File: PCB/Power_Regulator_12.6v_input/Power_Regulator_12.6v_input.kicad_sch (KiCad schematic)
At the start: 54 parts, among them J1 SE2-30, J2 Jack-DC, U1 TLP3542, U2 TPS55340RTER, U3 TPS563203, U4 TPS54JA20RWWR

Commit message: added test points
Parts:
- added J10, J12, J13, J4, J5, J6, J7, J8, J9: Conn_01x01_Pin, TestPoint:TestPoint_Pad_D1.0mm, symbol Connector:Conn_01x01_Pin
- added J3: Conn_01x05_Pin, Connector_PinHeader_2.54mm:PinHeader_1x05_P2.54mm_Vertical, symbol Connector:Conn_01x05_Pin
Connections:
- net +24V: now also J7.1 (Pin_1)
- net +3.3VA: now also J13.1 (Pin_1), J3.3 (Pin_3), J5.1 (Pin_1)
- net +5V: now also J10.1 (Pin_1), J3.4 (Pin_4), J4.1 (Pin_1)
- net +BATT: now also J3.2 (Pin_2), J8.1 (Pin_1), J9.1 (Pin_1)
- net 24V_RAW: now also J3.5 (Pin_5), J6.1 (Pin_1)
- net GND: now also J3.1 (Pin_1)
- net at R3.2, U1.1: now also J12.1 (Pin_1)

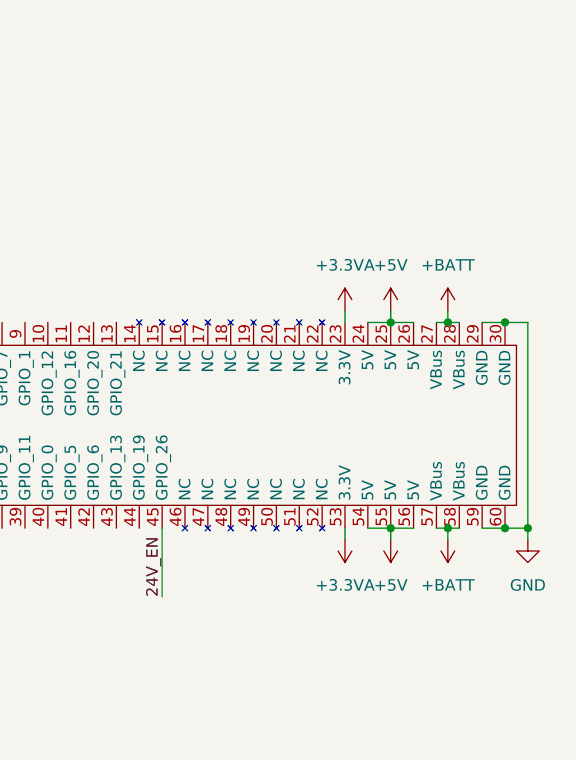
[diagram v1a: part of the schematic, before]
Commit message: added switch footprint
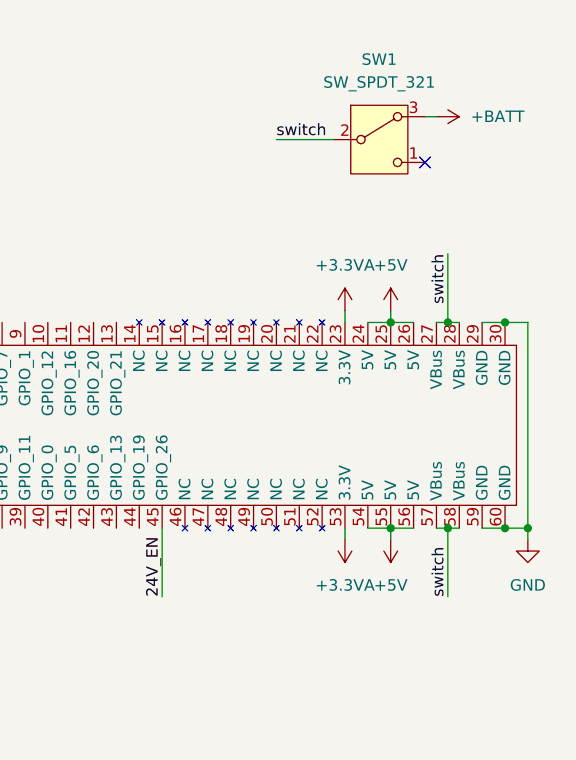
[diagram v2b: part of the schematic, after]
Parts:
- added SW1: SW_SPDT_321, symbol Switch:SW_SPDT_321
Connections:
- net +BATT: now also SW1.3 (A); no longer J1.27 (VBus), J1.28 (VBus), J1.57 (VBus), J1.58 (VBus)
- new net switch: J1.27 (VBus), J1.28 (VBus), J1.57 (VBus), J1.58 (VBus), SW1.2 (B)
- no-connect marks 0 -> 1
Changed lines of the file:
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@@
 		(color 0 0 0 0)
 	)
+	(no_connect
+		(at 270.51 29.21)
+	)
 	(wire
 		(pts
@@
 	(wire
 		(pts
+			(xy 254 26.67) (xy 260.35 26.67)
+		)
+		(stroke
+			(width 0)
+			(type default)
+		)
+	)
+	(wire
+		(pts
 			(xy 143.51 46.99) (xy 151.13 46.99)
 		)
@@
 	(wire
 		(pts
+			(xy 270.51 24.13) (xy 271.78 24.13)
+		)
+		(stroke
+			(width 0)
+			(type default)
+		)
+	)
+	(wire
+		(pts
 			(xy 86.36 160.02) (xy 64.77 160.02)
 		)
@@
 	(wire
 		(pts
-			(xy 273.05 71.12) (xy 273.05 69.85)
+			(xy 273.05 77.47) (xy 273.05 69.85)
 		)
 		(stroke
@@
 	(wire
 		(pts
-			(xy 273.05 45.72) (xy 273.05 46.99)
+			(xy 273.05 39.37) (xy 273.05 46.99)
 		)
 		(stroke
@@
 		)
 	)
+	(label "switch"
+		(at 254 26.67 0)
+		(effects
+			(font
+				(size 1.27 1.27)
+			)
+			(justify left bottom)
+		)
+	)
 	(label "24V_EN"
 		(at 17.78 184.15 0)
@@
 		)
 	)
+	(label "switch"
+		(at 273.05 77.47 90)
+		(effects
+			(font
+				(size 1.27 1.27)
+			)
+			(justify left bottom)
+		)
+	)
 	(label "24V_RAW"
 		(at 73.66 189.23 180)
@@
 		)
 	)
+	(label "switch"
+		(at 273.05 39.37 270)
+		(effects
+			(font
+				(size 1.27 1.27)
+			)
+			(justify right bottom)
+		)
+	)
 	(label "24V_EN"
 		(at 241.3 77.47 90)
@@
 	)
 	(symbol
-		(lib_id "power:+BATT")
-		(at 273.05 45.72 0)
-		(unit 1)
-		(exclude_from_sim no)
-		(in_bom yes)
-		(on_board yes)
-		(dnp no)
-		(fields_autoplaced yes)
-		(property "Reference" "#PWR05"
-			(at 273.05 49.53 0)
-			(effects
-				(font
-					(size 1.27 1.27)
-				)
-				(hide yes)
-			)
-		)
-		(property "Value" "+BATT"
-			(at 273.05 40.64 0)
-			(effects
-				(font
-					(size 1.27 1.27)
-				)
-			)
-		)
-		(property "Footprint" ""
-			(at 273.05 45.72 0)
-			(effects
-				(font
-					(size 1.27 1.27)
-				)
-				(hide yes)
-			)
-		)
-		(property "Datasheet" ""
-			(at 273.05 45.72 0)
-			(effects
-				(font
-					(size 1.27 1.27)
-				)
-				(hide yes)
-			)
-		)
-		(property "Description" "Power symbol creates a global label with name \"+BATT\""
-			(at 273.05 45.72 0)
-			(effects
-				(font
-					(size 1.27 1.27)
-				)
-				(hide yes)
-			)
-		)
-		(pin "1"
-		)
-		(instances
-			(project ""
-				(path "/3e19382a-168a-41e3-8127-b0b5a7558ca8"
-					(reference "#PWR05")
-					(unit 1)
-				)
-			)
-		)
-	)
-	(symbol
 		(lib_id "SE2-30:SE2-30")
 		(at 242.57 48.26 0)
@@
 	)
 	(symbol
+		(lib_id "power:+BATT")
+		(at 271.78 24.13 270)
+		(unit 1)
+		(exclude_from_sim no)
+		(in_bom yes)
+		(on_board yes)
+		(dnp no)
+		(fields_autoplaced yes)
+		(property "Reference" "#PWR05"
+			(at 267.97 24.13 0)
+			(effects
+				(font
+					(size 1.27 1.27)
+				)
+				(hide yes)
+			)
+		)
+		(property "Value" "+BATT"
+			(at 275.59 24.1299 90)
+			(effects
+				(font
+					(size 1.27 1.27)
+				)
+				(justify left)
+			)
+		)
+		(property "Footprint" ""
+			(at 271.78 24.13 0)
+			(effects
+				(font
+					(size 1.27 1.27)
+				)
+				(hide yes)
+			)
+		)
+		(property "Datasheet" ""
+			(at 271.78 24.13 0)
+			(effects
+				(font
+					(size 1.27 1.27)
+				)
+				(hide yes)
+			)
+		)
+		(property "Description" "Power symbol creates a global label with name \"+BATT\""
+			(at 271.78 24.13 0)
+			(effects
+				(font
+					(size 1.27 1.27)
+				)
+				(hide yes)
+			)
+		)
+		(pin "1"
+		)
+		(instances
+			(project ""
+				(path "/3e19382a-168a-41e3-8127-b0b5a7558ca8"
+					(reference "#PWR05")
+					(unit 1)
+				)
+			)
+		)
+	)
+	(symbol
 		(lib_id "Relay_SolidState:TLP3542")
 		(at 52.07 186.69 0)
@@
 	)
 	(symbol
+		(lib_id "Switch:SW_SPDT_321")
+		(at 265.43 26.67 0)
+		(unit 1)
+		(exclude_from_sim no)
+		(in_bom yes)
+		(on_board yes)
+		(dnp no)
+		(fields_autoplaced yes)
+		(property "Reference" "SW1"
+			(at 265.43 17.78 0)
+			(effects
+				(font
+					(size 1.27 1.27)
+				)
+			)
+		)
+		(property "Value" "SW_SPDT_321"
+			(at 265.43 20.32 0)
+			(effects
+				(font
+					(size 1.27 1.27)
+				)
+			)
+		)
+		(property "Footprint" ""
+			(at 265.43 36.83 0)
+			(effects
+				(font
+					(size 1.27 1.27)
+				)
+				(hide yes)
+			)
+		)
+		(property "Datasheet" "~"
+			(at 265.43 34.29 0)
+			(effects
+				(font
+					(size 1.27 1.27)
+				)
+				(hide yes)
+			)
+		)
+		(property "Description" "Switch, single pole double throw"
+			(at 265.43 26.67 0)
+			(effects
+				(font
+					(size 1.27 1.27)
+				)
+				(hide yes)
+			)
+		)
+		(pin "2"
+		)
+		(pin "1"
+		)
+		(pin "3"
+		)
+		(instances
+			(project ""
+				(path "/3e19382a-168a-41e3-8127-b0b5a7558ca8"
+					(reference "SW1")
+					(unit 1)
+				)
+			)
+		)
+	)
+	(symbol
 		(lib_id "power:GND")
 		(at 144.78 189.23 270)
@@
 					(unit 1)
 				)
-			)
-		)
-	)
-	(symbol
-		(lib_id "power:+BATT")
-		(at 273.05 71.12 180)
-		(unit 1)
-		(exclude_from_sim no)
-		(in_bom yes)
-		(on_board yes)
-		(dnp no)
-		(fields_autoplaced yes)
-		(property "Reference" "#PWR06"
-			(at 273.05 67.31 0)
-			(effects
-				(font
-					(size 1.27 1.27)
-				)
-				(hide yes)
-			)
-		)
-		(property "Value" "+BATT"
-			(at 273.05 76.2 0)
-			(effects
-				(font
-					(size 1.27 1.27)
-				)
-			)
-		)
-		(property "Footprint" ""
-			(at 273.05 71.12 0)
-			(effects
-				(font
-					(size 1.27 1.27)
-				)
-				(hide yes)
-			)
-		)
-		(property "Datasheet" ""
-			(at 273.05 71.12 0)
-			(effects
-				(font
-					(size 1.27 1.27)
-				)
-				(hide yes)
-			)
-		)
-		(property "Description" "Power symbol creates a global label with name \"+BATT\""
-			(at 273.05 71.12 0)
-			(effects
-				(font
-					(size 1.27 1.27)
-				)
-				(hide yes)
-			)
-		)
-		(pin "1"
-		)
-		(instances
-			(project "Power_Regulator_12.6v_input"
-				(path "/3e19382a-168a-41e3-8127-b0b5a7558ca8"
-					(reference "#PWR06")
-					(unit 1)
-				)

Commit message: added connector and switch
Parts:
- J2: footprint (none) -> XT-Conn:AMASS_XT60-M_1x02_P7.20mm_Vertical
- SW1: footprint (none) -> SS-5:SS-5
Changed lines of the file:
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@@
 			)
 		)
-		(property "Footprint" ""
+		(property "Footprint" "SS-5:SS-5"
 			(at 265.43 36.83 0)
 			(effects
@@
 			)
 		)
-		(property "Footprint" ""
+		(property "Footprint" "XT-Conn:AMASS_XT60-M_1x02_P7.20mm_Vertical"
 			(at 105.41 184.404 0)
 			(effects
